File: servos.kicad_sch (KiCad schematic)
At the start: 12 parts, among them J10 171857-0003, J7 171857-0003, J8 171857-0003, J9 171857-0003

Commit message: sisyphus goes hard, awaiting review.
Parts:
- renumbered J9 to J10, J10 to J11, J7 to J8, J8 to J9, R11 to R13, R12 to R14, R13 to R15, R14 to R16, R15 to R17, R16 to R18, R17 to R19, R18 to R20
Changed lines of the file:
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@@
 		(dnp no)
 		(fields_autoplaced yes)
-		(property "Reference" "R14"
+		(property "Reference" "R16"
 			(at 115.57 116.84 0)
 			(show_name no)
@@
 			(project "engineering_plane"
 				(path "/f9a2ded0-d803-4be9-b2f5-4dda0f6b4d9a/a8884140-4da9-49d2-8de3-8d91ee78d46d"
-					(reference "R14")
+					(reference "R16")
 					(unit 1)
 				)
@@
 		(dnp no)
 		(fields_autoplaced yes)
-		(property "Reference" "R13"
+		(property "Reference" "R15"
 			(at 115.57 88.9 0)
 			(show_name no)
@@
 			(project "engineering_plane"
 				(path "/f9a2ded0-d803-4be9-b2f5-4dda0f6b4d9a/a8884140-4da9-49d2-8de3-8d91ee78d46d"
-					(reference "R13")
+					(reference "R15")
 					(unit 1)
 				)
@@
 		(dnp no)
 		(fields_autoplaced yes)
-		(property "Reference" "J7"
+		(property "Reference" "J8"
 			(at 149.86 49.5299 0)
 			(show_name no)
@@
 			(project "engineering_plane"
 				(path "/f9a2ded0-d803-4be9-b2f5-4dda0f6b4d9a/a8884140-4da9-49d2-8de3-8d91ee78d46d"
-					(reference "J7")
+					(reference "J8")
 					(unit 1)
 				)
@@
 		(dnp no)
 		(fields_autoplaced yes)
-		(property "Reference" "J10"
+		(property "Reference" "J11"
 			(at 149.86 124.4599 0)
 			(show_name no)
@@
 			(project "engineering_plane"
 				(path "/f9a2ded0-d803-4be9-b2f5-4dda0f6b4d9a/a8884140-4da9-49d2-8de3-8d91ee78d46d"
-					(reference "J10")
+					(reference "J11")
 					(unit 1)
 				)
@@
 		(dnp no)
 		(fields_autoplaced yes)
-		(property "Reference" "J8"
+		(property "Reference" "J9"
 			(at 149.86 74.9299 0)
 			(show_name no)
@@
 			(project "engineering_plane"
 				(path "/f9a2ded0-d803-4be9-b2f5-4dda0f6b4d9a/a8884140-4da9-49d2-8de3-8d91ee78d46d"
-					(reference "J8")
+					(reference "J9")
 					(unit 1)
 				)
@@
 		(dnp no)
 		(fields_autoplaced yes)
-		(property "Reference" "R11"
+		(property "Reference" "R13"
 			(at 115.57 41.91 0)
 			(show_name no)
@@
 			(project "engineering_plane"
 				(path "/f9a2ded0-d803-4be9-b2f5-4dda0f6b4d9a/a8884140-4da9-49d2-8de3-8d91ee78d46d"
-					(reference "R11")
+					(reference "R13")
 					(unit 1)
 				)
@@
 		(dnp no)
 		(fields_autoplaced yes)
-		(property "Reference" "R15"
+		(property "Reference" "R17"
 			(at 124.46 50.7999 90)
 			(show_name no)
@@
 			(project "engineering_plane"
 				(path "/f9a2ded0-d803-4be9-b2f5-4dda0f6b4d9a/a8884140-4da9-49d2-8de3-8d91ee78d46d"
-					(reference "R15")
+					(reference "R17")
 					(unit 1)
 				)
@@
 		(dnp no)
 		(fields_autoplaced yes)
-		(property "Reference" "R17"
+		(property "Reference" "R19"
 			(at 124.46 97.7899 90)
 			(show_name no)
@@
 			(project "engineering_plane"
 				(path "/f9a2ded0-d803-4be9-b2f5-4dda0f6b4d9a/a8884140-4da9-49d2-8de3-8d91ee78d46d"
-					(reference "R17")
+					(reference "R19")
 					(unit 1)
 				)
@@
 		(dnp no)
 		(fields_autoplaced yes)
-		(property "Reference" "R18"
+		(property "Reference" "R20"
 			(at 124.46 125.7299 90)
 			(show_name no)
@@
 			(project "engineering_plane"
 				(path "/f9a2ded0-d803-4be9-b2f5-4dda0f6b4d9a/a8884140-4da9-49d2-8de3-8d91ee78d46d"
-					(reference "R18")
+					(reference "R20")
 					(unit 1)
 				)
@@
 		(dnp no)
 		(fields_autoplaced yes)
-		(property "Reference" "J9"
+		(property "Reference" "J10"
 			(at 149.86 96.5199 0)
 			(show_name no)
@@
 			(project "engineering_plane"
 				(path "/f9a2ded0-d803-4be9-b2f5-4dda0f6b4d9a/a8884140-4da9-49d2-8de3-8d91ee78d46d"
-					(reference "J9")
+					(reference "J10")
 					(unit 1)
 				)
@@
 		(dnp no)
 		(fields_autoplaced yes)
-		(property "Reference" "R16"
+		(property "Reference" "R18"
 			(at 124.46 76.1999 90)
 			(show_name no)
@@
 			(project "engineering_plane"
 				(path "/f9a2ded0-d803-4be9-b2f5-4dda0f6b4d9a/a8884140-4da9-49d2-8de3-8d91ee78d46d"
-					(reference "R16")
+					(reference "R18")
 					(unit 1)
 				)
@@
 		(dnp no)
 		(fields_autoplaced yes)
-		(property "Reference" "R12"
+		(property "Reference" "R14"
 			(at 115.57 67.31 0)
 			(show_name no)
@@
 			(project "engineering_plane"
 				(path "/f9a2ded0-d803-4be9-b2f5-4dda0f6b4d9a/a8884140-4da9-49d2-8de3-8d91ee78d46d"
-					(reference "R12")
-					(unit 1)
-				)
+					(reference "R14")
+					(unit 1)
+				)

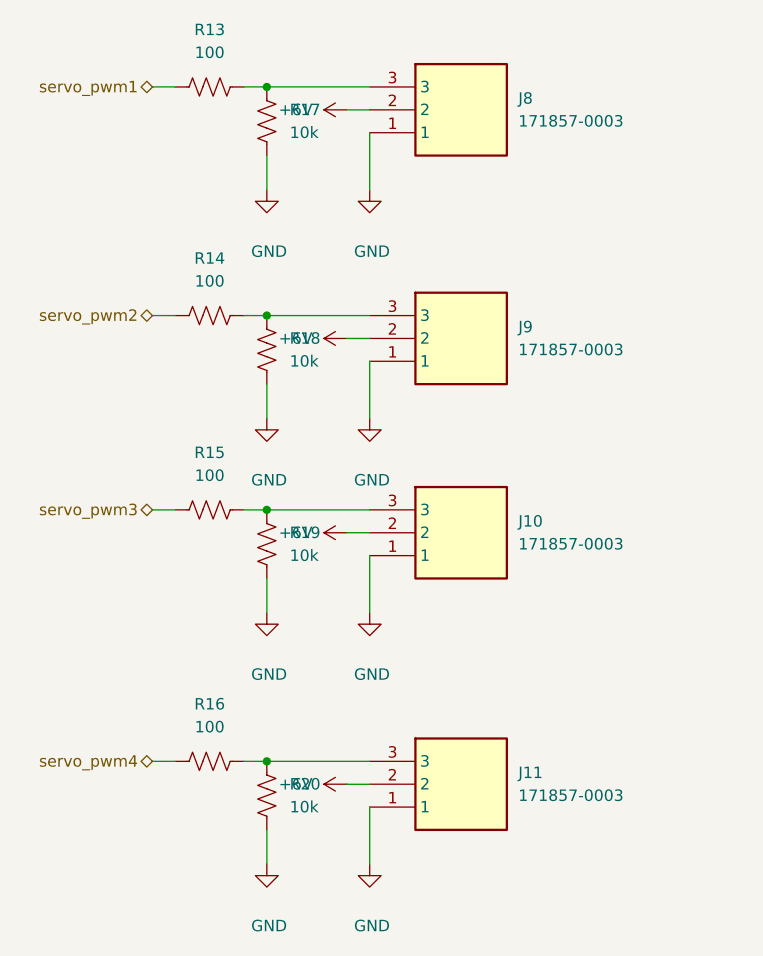
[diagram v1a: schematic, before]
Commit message: feat: rev1 added sdcard
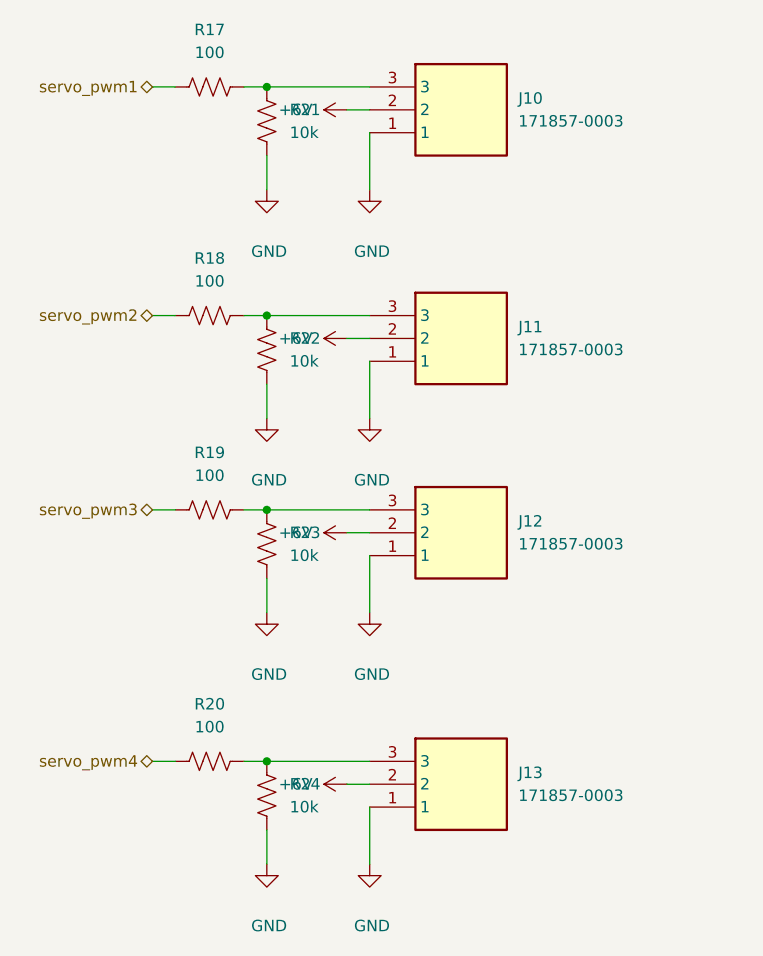
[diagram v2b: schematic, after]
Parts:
- renumbered J8 to J10, J9 to J11, J10 to J12, J11 to J13, R13 to R17, R14 to R18, R15 to R19, R16 to R20, R17 to R21, R18 to R22, R19 to R23, R20 to R24

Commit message: feat: final changes, sent to prod
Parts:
- R13: renamed from R17; value 100 -> 22
- R14: renamed from R18; value 100 -> 22
- R15: renamed from R19; value 100 -> 22
- R16: renamed from R20; value 100 -> 22
- renumbered J10 to J11, J11 to J12, J12 to J13, J13 to J14, R21 to R17, R22 to R18, R23 to R19, R24 to R20

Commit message: Revised componenents, need to route
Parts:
- removed R13, R14, R15, R16: 22, PCM_SparkFun-Resistor:R_0603_1608Metric, symbol PCM_SparkFun-Resistor:R
- removed R17, R18, R19, R20: 10k, PCM_SparkFun-Resistor:R_0603_1608Metric, symbol PCM_SparkFun-Resistor:R
- added R401, R402, R403, R404: 22Ω, PCM_JLCPCB:R_0402, symbol PCM_JLCPCB-Resistors:0402,22Ω
- added R405, R406, R407, R408: 10kΩ, PCM_JLCPCB:R_0402, symbol PCM_JLCPCB-Resistors:0402,10kΩ
- renumbered J11 to J401, J12 to J402, J13 to J403, J14 to J404
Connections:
- net GND: now also R405.2, R406.2, R407.2, R408.2
- net servo_pwm1: now also R401.1
- net servo_pwm2: now also R402.1
- net servo_pwm3: now also R403.1
- net servo_pwm4: now also R404.1
- net at J404.3: now also R404.2, R408.1
- net at J403.3: now also R403.2, R407.1
- net at J401.3: now also R401.2, R405.1
- net at J402.3: now also R402.2, R406.1

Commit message: rev2 additional thingis
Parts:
- removed J401, J402, J403, J404: 171857-0003, eng_plane_lib:1718570003, symbol eng_plane_lib:171857-0003
- added J401, J402, J403, J404: S3B-XH-A-1__LF__SN_, eng_plane_lib:S3BXHA1LFSN, symbol eng_plane_lib:S3B-XH-A-1__LF__SN_
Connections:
- net +6V: now also J401.2, J402.2, J403.2, J404.2
- net GND: now also J401.1, J402.1, J403.1, J404.1
- net at R404.2, R408.1: now also J404.3
- net at R402.2, R406.1: now also J402.3
- net at R401.2, R405.1: now also J401.3
- net at R403.2, R407.1: now also J403.3
